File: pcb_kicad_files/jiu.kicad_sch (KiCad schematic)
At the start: 170 parts, among them J1 TYPE-C-31-M-12, J2 ARM JTAG, Q1 DTC123JKAT146, SW1 1U, SW10 1U, SW11 1U, SW12 1U, SW13 1U, SW14 1U, SW15 1U, SW16 2u, SW17 1.5U, SW18 1U, SW19 1U, SW2 1U, SW20 1U, SW21 1U, SW22 1U, SW23 1U, SW24 1U, SW25 1U, SW26 1U, SW27 1U, SW28 1U, SW29 1U, SW3 1U, SW30 1.5U, SW31 1U, SW32 1.75U, SW33 1U, SW34 1U, SW35 1U, SW36 1U, SW37 1U, SW38 1U, SW39 1U, SW4 1U, SW40 1U, SW41 1U, SW42 1U, SW43 1U, SW44 2.25U, SW45 1U, SW46 2.25U, SW47 1.25U, SW48 1U, SW49 1U, SW5 1U, SW50 1U, SW51 1U, SW52 1U, SW53 1U, SW54 1U, SW55 1U, SW56 1U, SW57 1.75U, SW58 1U, SW59 1U, SW6 1U, SW60 1.5U, SW61 1U, SW62 1.5U, SW63 7U, SW64 1U, SW65 1.5U, SW66 1U, SW67 K2-1187SQ-A4SW-06, SW68 1U, SW69 1U, SW7 1U, SW70 1.25U, SW71 1.25U, SW72 1.25U, SW73 6.25U, SW74 1.25U, SW8 1U, SW9 1U, U1 MCP1700T-3302E/TT, U2 STM32F072CBT6

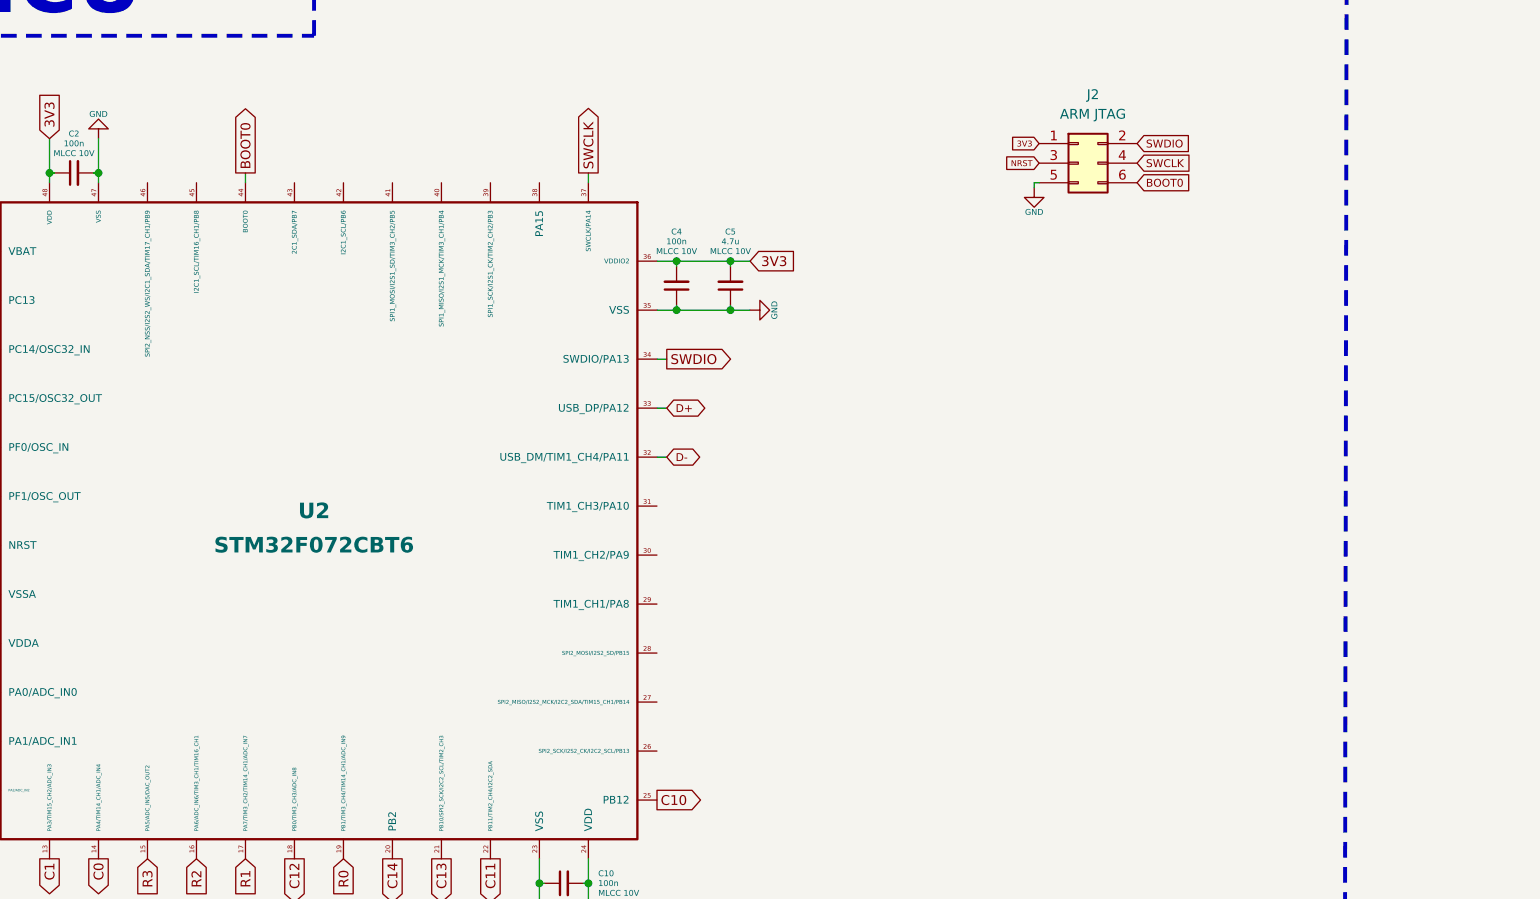
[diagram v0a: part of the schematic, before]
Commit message: Added pin header esposing extra unused MCU pins
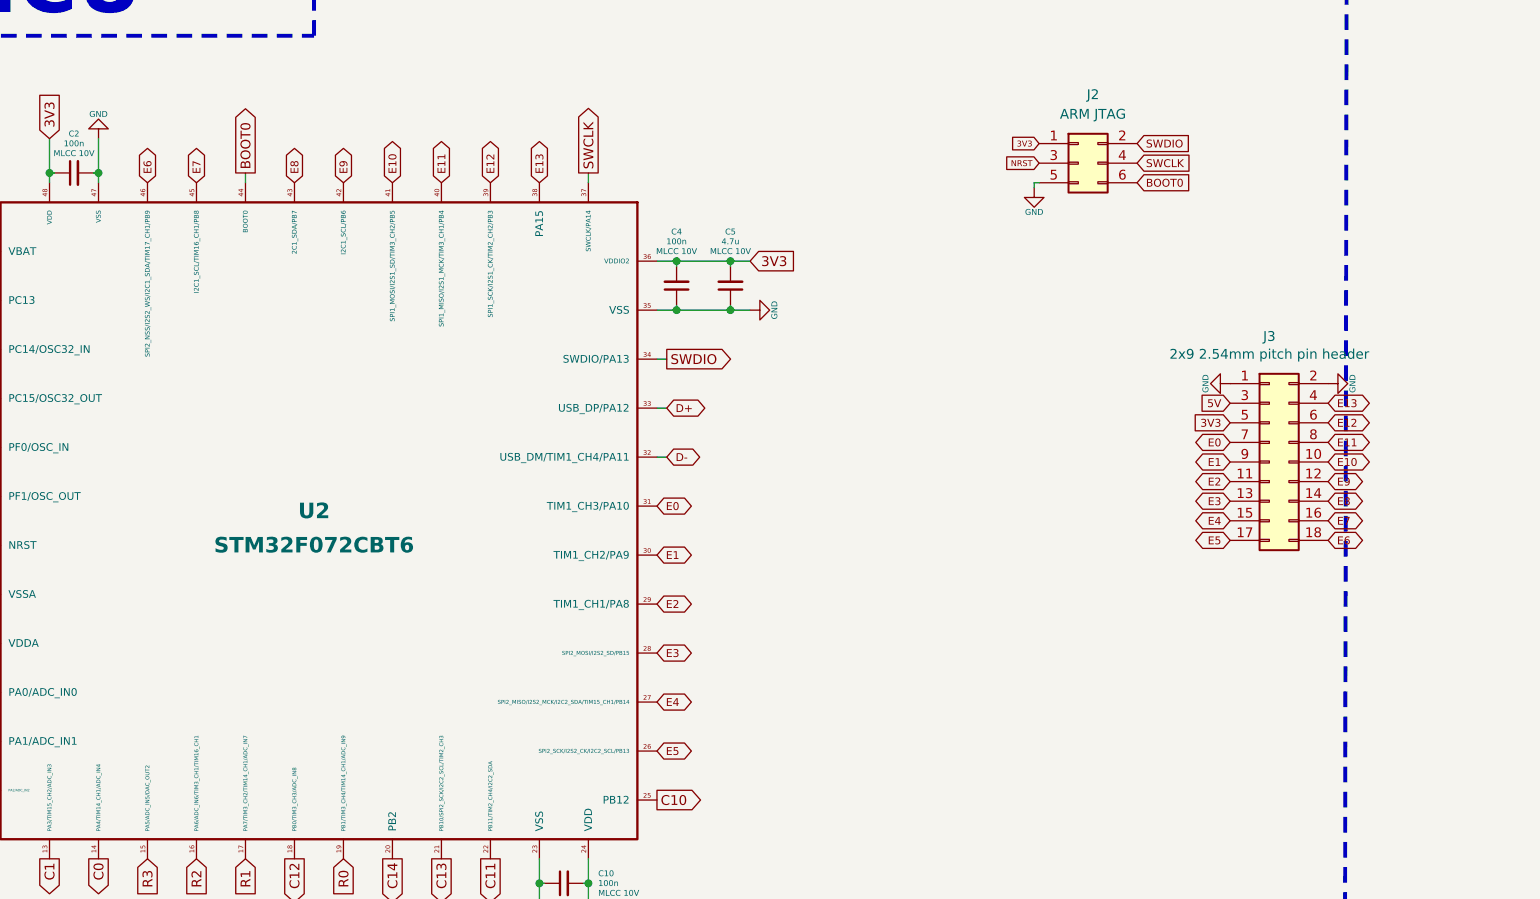
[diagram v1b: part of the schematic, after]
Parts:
- added J3: 2x9 2.54mm pitch pin header, acheron_Connectors:PinHeader_2x9_P2.54mm_Vertical, symbol Connector_Generic:Conn_02x09_Odd_Even
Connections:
- net 3V3: now also J3.5 (Pin_5)
- net 5V: now also J3.3 (Pin_3)
- net GND: now also J3.1 (Pin_1), J3.2 (Pin_2)
- net E5: now reaches U2.26 (SPI2_SCK/I2S2_CK/I2C2_SCL/PB13)
- net E5: now also J3.17 (Pin_17)
- net E4: now reaches U2.27 (SPI2_MISO/I2S2_MCK/I2C2_SDA/TIM15_CH1/PB14)
- net E4: now also J3.15 (Pin_15)
- net E3: now reaches U2.28 (SPI2_MOSI/I2S2_SD/PB15)
- net E3: now also J3.13 (Pin_13)
- net E2: now reaches U2.29 (TIM1_CH1/PA8)
- net E2: now also J3.11 (Pin_11)
- net E1: now reaches U2.30 (TIM1_CH2/PA9)
- net E1: now also J3.9 (Pin_9)
- net E0: now reaches U2.31 (TIM1_CH3/PA10)
- net E0: now also J3.7 (Pin_7)
- net E13: now reaches U2.38 (PA15)
- net E13: now also J3.4 (Pin_4)
- net E12: now reaches U2.39 (SPI1_SCK/I2S1_CK/TIM2_CH2/PB3)
- net E12: now also J3.6 (Pin_6)
- net E11: now reaches U2.40 (SPI1_MISO/I2S1_MCK/TIM3_CH1/PB4)
- net E11: now also J3.8 (Pin_8)
- net E10: now reaches U2.41 (SPI1_MOSI/I2S1_SD/TIM3_CH2/PB5)
- net E10: now also J3.10 (Pin_10)
- net E9: now reaches U2.42 (I2C1_SCL/PB6)
- net E9: now also J3.12 (Pin_12)
- net E8: now reaches U2.43 (2C1_SDA/PB7)
- net E8: now also J3.14 (Pin_14)
- net E7: now reaches U2.45 (I2C1_SCL/TIM16_CH1/PB8)
- net E7: now also J3.16 (Pin_16)
- net E6: now reaches U2.46 (SPI2_NSS/I2S2_WS/I2C1_SDA/TIM17_CH1/PB9)
- net E6: now also J3.18 (Pin_18)

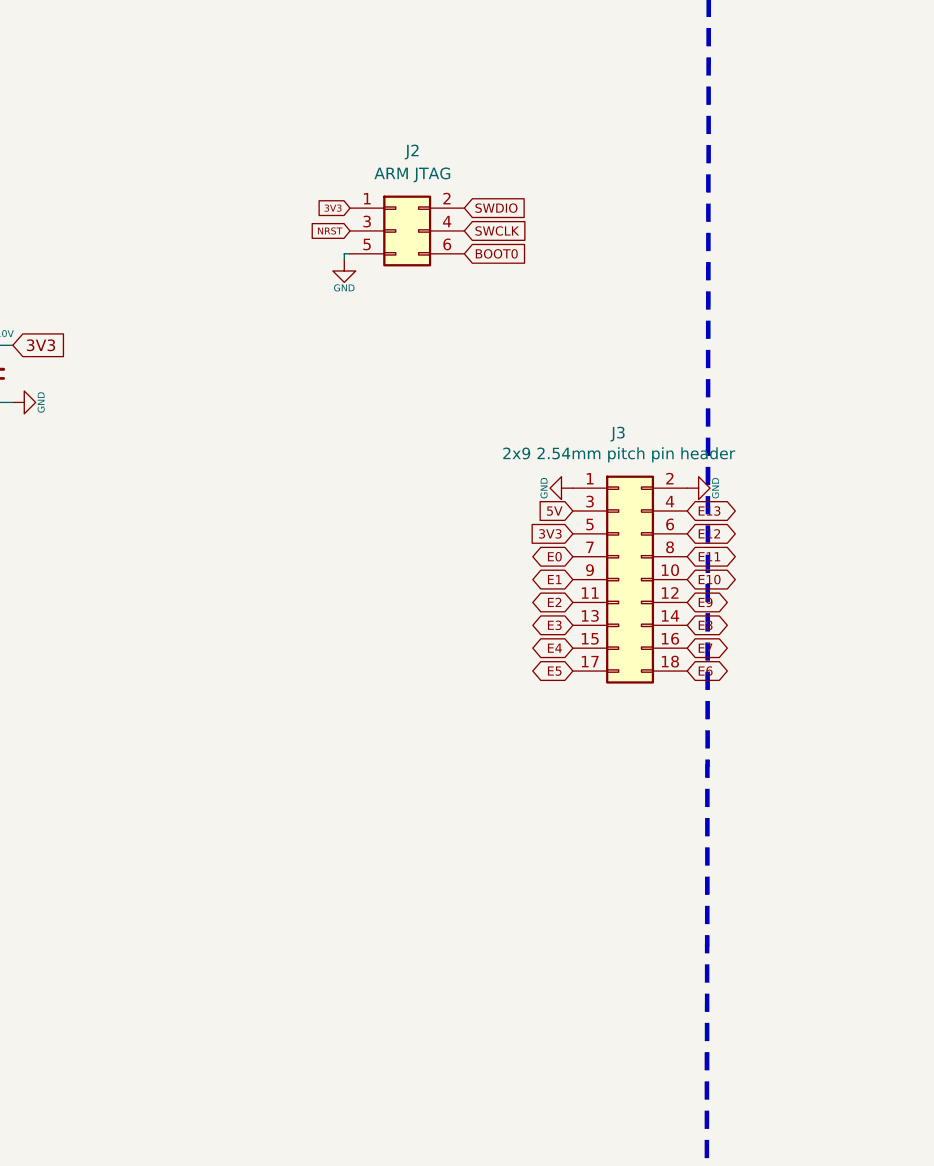
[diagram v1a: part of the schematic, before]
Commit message: Add pin header for rows
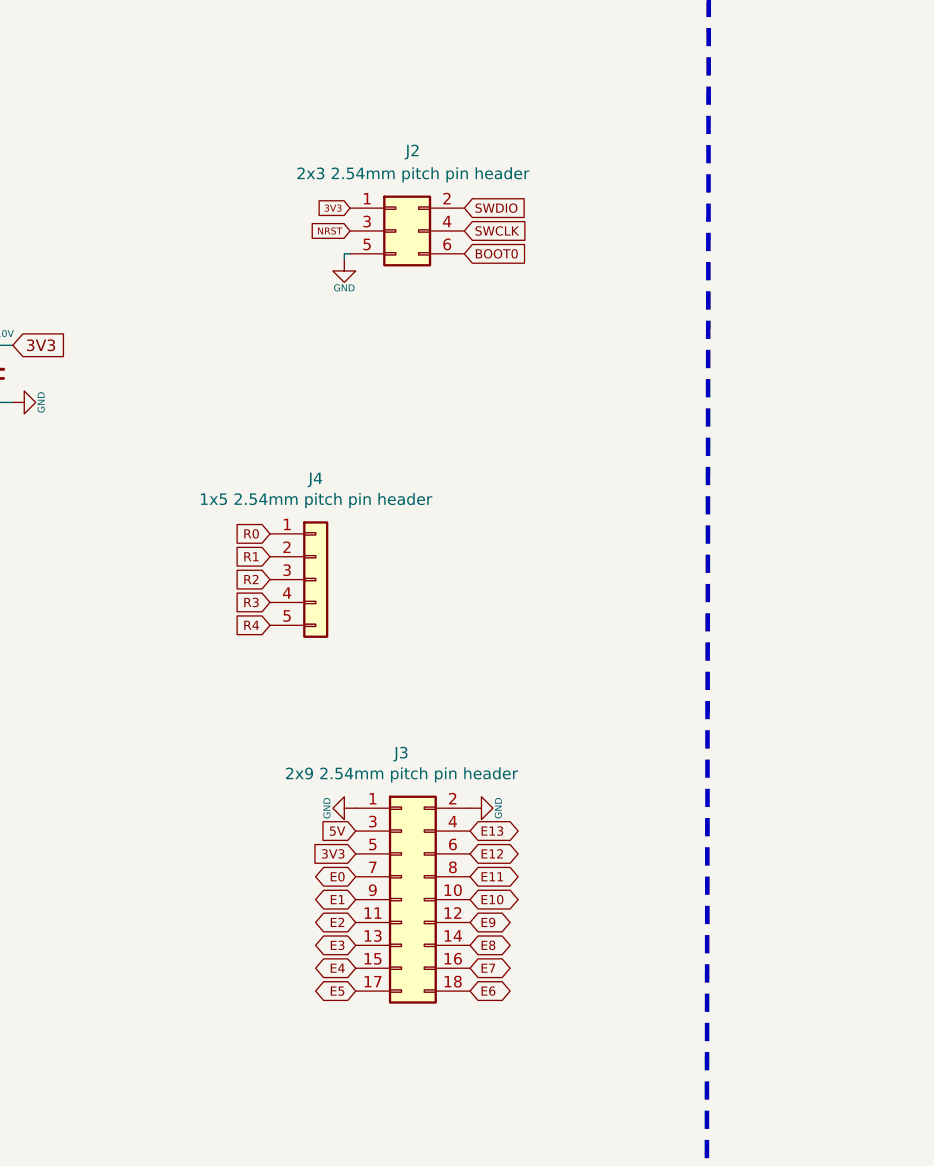
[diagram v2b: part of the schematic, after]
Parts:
- added J4: 1x5 2.54mm pitch pin header, acheron_Connectors:PinHeader_1x5_P2.54mm_Vertical, symbol Connector_Generic:Conn_01x05
- J2: value ARM JTAG -> 2x3 2.54mm pitch pin header
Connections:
- net R0: now also J4.1 (Pin_1)
- net R1: now also J4.2 (Pin_2)
- net R2: now also J4.3 (Pin_3)
- net R3: now also J4.4 (Pin_4)
- net R4: now also J4.5 (Pin_5)
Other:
- moved on the sheet: J3

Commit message: Added USBLC chip, removed discrete TVS, organized LDO circuitry
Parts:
- removed D17: SMF6.0A, acheron_Components:D_SOD-123, symbol Device:D_Schottky
- added U1: USBLC6-2SC6, acheron_Components:SOT-23-6, symbol Power_Protection:USBLC6-2SC6
- renumbered C7 to C10, C10 to C11, C11 to C12, C12 to C4, C4 to C5, C5 to C6, C8 to C7, C9 to C8, C6 to C9, D11 to D10, D12 to D11, D14 to D12, D15 to D13, D16 to D14, D18 to D15, D19 to D16, D20 to D17, D21 to D18, D22 to D19, D23 to D20, D25 to D21, D26 to D22, D27 to D23, D28 to D24, D29 to D25, D30 to D26, D32 to D27, D33 to D28, D35 to D29, D36 to D30, D37 to D31, D38 to D32, D39 to D33, D40 to D34, D41 to D35, D42 to D36, D44 to D37, D45 to D38, D46 to D39, D47 to D40, D48 to D41, D50 to D42, D51 to D43, D53 to D44, D54 to D45, D55 to D46, D56 to D47, D57 to D48, D58 to D49, D60 to D50, D61 to D51, D62 to D52, D63 to D53, D64 to D54, D65 to D55, D66 to D56, D78 to D57, D69 to D58, D70 to D59, D7 to D6, D71 to D60, D72 to D61, D73 to D62, D75 to D63, D80 to D64, D76 to D65, D82 to D66, D6 to D67, D13 to D68, D8 to D7, D9 to D8, D10 to D9, J2 to J1, J1 to J2, J4 to J3, J3 to J4, R3 to R1, R1 to R2, R2 to R3, SW47 to SW46, SW46 to SW47, SW59 to SW48, SW48 to SW49, SW49 to SW50, SW50 to SW51, SW51 to SW52, SW52 to SW53, SW53 to SW54, SW54 to SW55, SW55 to SW56, SW56 to SW57, SW57 to SW58, SW68 to SW59, SW58 to SW60, SW60 to SW61, SW61 to SW62, SW62 to SW63, SW63 to SW64, SW69 to SW66, SW64 to SW67, SW66 to SW68, SW70 to SW69, SW71 to SW70, SW72 to SW71, SW73 to SW72, SW74 to SW73, SW67 to SW74, U1 to U3
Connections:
- net D+: now also U1.3 (I/O2); no longer J2.A6 (D+), J2.B6 (D+)
- net D-: now also U1.1 (I/O1); no longer J2.A7 (D-), J2.B7 (D-)
- net GND: now also U1.2 (GND)
- net VUSB: now also U1.5 (VBUS)
- new net DBUS+: J2.A6 (D+), J2.B6 (D+), U1.4 (I/O2)
- new net DBUS-: J2.A7 (D-), J2.B7 (D-), U1.6 (I/O1)

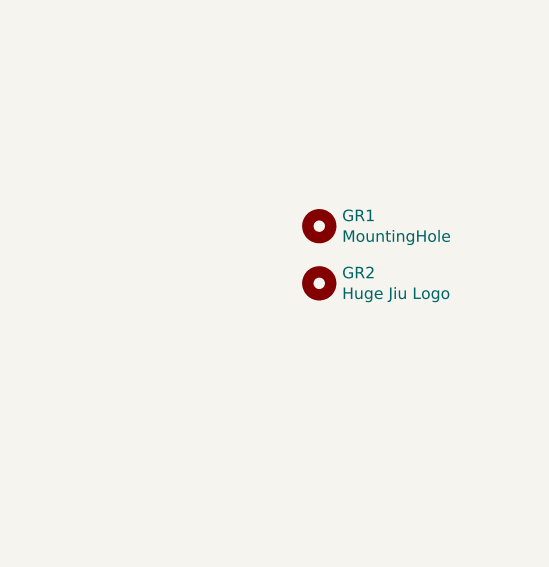
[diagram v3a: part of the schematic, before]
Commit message: Add Acheron Plated logo to PCB front
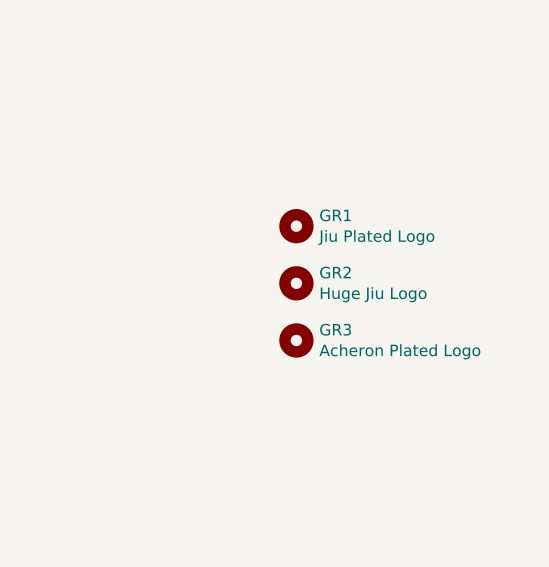
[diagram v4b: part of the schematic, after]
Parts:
- added GR3: Acheron Plated Logo, acheron_Logos:acheronShort_0.3x0.5in_Plated, symbol Mechanical:MountingHole
- GR1: value MountingHole -> Jiu Plated Logo
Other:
- moved on the sheet: GR1, GR2
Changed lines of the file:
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@@
     (title "Jiu schematic")
     (date "2021-01-13")
-    (rev "v1.1.2")
+    (rev "v1.1.3-c1")
     (company "Designed by Gondolindrim")
   )
@@
     )
   )
-  (symbol (lib_id "Mechanical:MountingHole") (at 497.84 171.45 0) (unit 1)
+  (symbol (lib_id "Mechanical:MountingHole") (at 495.3 171.45 0) (unit 1)
     (in_bom no) (on_board yes)
-    (property "Reference" "GR1" (id 0) (at 500.3801 170.3006 0)
+    (property "Reference" "GR1" (id 0) (at 497.8401 170.3006 0)
       (effects (font (size 1.27 1.27)) (justify left))
     )
-    (property "Value" "MountingHole" (id 1) (at 500.3801 172.5993 0)
+    (property "Value" "Jiu Plated Logo" (id 1) (at 497.8401 172.5993 0)
       (effects (font (size 1.27 1.27)) (justify left))
     )
-    (property "Footprint" "jiu_graphics:jiu_logo_15.9x15.0mm" (id 2) (at 497.84 171.45 0)
+    (property "Footprint" "jiu_graphics:jiu_logo_15.9x15.0mm" (id 2) (at 495.3 171.45 0)
       (effects (font (size 1.27 1.27)) hide)
     )
-    (property "Datasheet" "~" (id 3) (at 497.84 171.45 0)
+    (property "Datasheet" "~" (id 3) (at 495.3 171.45 0)
       (effects (font (size 1.27 1.27)) hide)
     )
   )
-  (symbol (lib_id "Mechanical:MountingHole") (at 497.84 177.8 0) (unit 1)
+  (symbol (lib_id "Mechanical:MountingHole") (at 495.3 177.8 0) (unit 1)
     (in_bom no) (on_board yes)
-    (property "Reference" "GR2" (id 0) (at 500.3801 176.6506 0)
+    (property "Reference" "GR2" (id 0) (at 497.8401 176.6506 0)
       (effects (font (size 1.27 1.27)) (justify left))
     )
-    (property "Value" "Huge Jiu Logo" (id 1) (at 500.3801 178.9493 0)
+    (property "Value" "Huge Jiu Logo" (id 1) (at 497.8401 178.9493 0)
       (effects (font (size 1.27 1.27)) (justify left))
     )
-    (property "Footprint" "jiu_graphics:jiu_logo_80x75.6" (id 2) (at 497.84 177.8 0)
+    (property "Footprint" "jiu_graphics:jiu_logo_80x75.6" (id 2) (at 495.3 177.8 0)
       (effects (font (size 1.27 1.27)) hide)
     )
-    (property "Datasheet" "~" (id 3) (at 497.84 177.8 0)
+    (property "Datasheet" "~" (id 3) (at 495.3 177.8 0)
+      (effects (font (size 1.27 1.27)) hide)
+    )
+  )
+  (symbol (lib_id "Mechanical:MountingHole") (at 495.3 184.15 0) (unit 1)
+    (in_bom no) (on_board yes)
+    (property "Reference" "GR3" (id 0) (at 497.8401 183.0006 0)
+      (effects (font (size 1.27 1.27)) (justify left))
+    )
+    (property "Value" "Acheron Plated Logo" (id 1) (at 497.8401 185.2993 0)
+      (effects (font (size 1.27 1.27)) (justify left))
+    )
+    (property "Footprint" "acheron_Logos:acheronShort_0.3x0.5in_Plated" (id 2) (at 495.3 184.15 0)
+      (effects (font (size 1.27 1.27)) hide)
+    )
+    (property "Datasheet" "~" (id 3) (at 495.3 184.15 0)
       (effects (font (size 1.27 1.27)) hide)
     )
@@
     )
     (path "/0eef0c02-56dd-4af2-ab7e-8a661a917c89"
-      (reference "GR1") (unit 1) (value "MountingHole") (footprint "jiu_graphics:jiu_logo_15.9x15.0mm")
+      (reference "GR1") (unit 1) (value "Jiu Plated Logo") (footprint "jiu_graphics:jiu_logo_15.9x15.0mm")
     )
     (path "/c3a789f0-1bd3-4731-a466-0502f1b91899"
       (reference "GR2") (unit 1) (value "Huge Jiu Logo") (footprint "jiu_graphics:jiu_logo_80x75.6")
     )
+    (path "/595c22e3-12a7-4ffb-b454-35a27f64443c"
+      (reference "GR3") (unit 1) (value "Acheron Plated Logo") (footprint "acheron_Logos:acheronShort_0.3x0.5in_Plated")
+    )
     (path "/aecb07b2-9d27-41eb-8320-1ebe9ea13f34"

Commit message: Added metadata to some components
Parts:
- J2: LCSC Part Number (none) -> C165948; Manufacturer (none) -> Korean Hroparts; Manufacturer Part Number (none) -> TYPE-C-31-M-12; Specification (none) -> USB type C female 16 pin connector
- Q1: LCSC Part Number (none) -> C111724; Specification (none) -> NPN pre-biased 200mW BJT transistor
- U1: LCSC Part Number (none) -> C7519; Manufacturer (none) -> STMicroelectronics; Manufacturer Part Number (none) -> USBLC6-2SC6; Package (none) -> SOT-23-6; Specification (none) -> Unidirectional 6V 5A SOT-23-6 TVS diode for USB ESD protect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
- U2: Specification (none) -> 32-bit 128kB FLASH ARM Cortex-M0 48MHz
- U3: Specification (none) -> Fixed 3.3V low dropout regulator
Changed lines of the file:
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@@
     (title "Jiu schematic")
     (date "2021-01-13")
-    (rev "v1.1.3-c1")
+    (rev "v1.1.3-c2")
     (company "Designed by Gondolindrim")
   )
@@
       (effects (font (size 1.27 1.27)) hide)
     )
+    (property "LCSC Part Number" "C111724" (id 4) (at 187.325 267.97 0)
+      (effects (font (size 1.27 1.27)) hide)
+    )
+    (property "Specification" "NPN pre-biased 200mW BJT transistor" (id 5) (at 187.325 267.97 0)
+      (effects (font (size 1.27 1.27)) hide)
+    )
   )
   (symbol (lib_id "Regulator_Linear:MCP1700-3302E_SOT23") (at 204.47 334.645 0) (unit 1)
@@
       (effects (font (size 1.27 1.27)) hide)
     )
+    (property "Specification" "Fixed 3.3V low dropout regulator" (id 4) (at 204.47 334.645 0)
+      (effects (font (size 1.27 1.27)) hide)
+    )
   )
   (symbol (lib_id "acheronSymbols:MXSwitch") (at 50.8 50.8 90) (mirror x) (unit 1)
@@
       (effects (font (size 1.27 1.27)) hide)
     )
+    (property "LCSC Part Number" "C7519" (id 4) (at 52.705 239.395 0)
+      (effects (font (size 1.27 1.27)) hide)
+    )
+    (property "Manufacturer" "STMicroelectronics" (id 5) (at 52.705 239.395 0)
+      (effects (font (size 1.27 1.27)) hide)
+    )
+    (property "Manufacturer Part Number" "USBLC6-2SC6" (id 6) (at 52.705 239.395 0)
+      (effects (font (size 1.27 1.27)) hide)
+    )
+    (property "Package" "SOT-23-6" (id 7) (at 52.705 239.395 0)
+      (effects (font (size 1.27 1.27)) hide)
+    )
+    (property "Specification" "Unidirectional 6V 5A SOT-23-6 TVS diode for USB ESD protection" (id 8) (at 52.705 239.395 0)
+      (effects (font (size 1.27 1.27)) hide)
+    )
   )
   (symbol (lib_id "acheronSymbols:TYPE-C-31-M12_13") (at 99.06 289.56 0) (unit 1)
@@
       (effects (font (size 1.524 1.524)) hide)
     )
+    (property "LCSC Part Number" "C165948" (id 4) (at 99.06 289.56 0)
+      (effects (font (size 1.27 1.27)) hide)
+    )
+    (property "Manufacturer" "Korean Hroparts" (id 5) (at 99.06 289.56 0)
+      (effects (font (size 1.27 1.27)) hide)
+    )
+    (property "Manufacturer Part Number" "TYPE-C-31-M-12" (id 6) (at 99.06 289.56 0)
+      (effects (font (size 1.27 1.27)) hide)
+    )
+    (property "Specification" "USB type C female 16 pin connector" (id 7) (at 99.06 289.56 0)
+      (effects (font (size 1.27 1.27)) hide)
+    )
   )
   (symbol (lib_id "acheronSymbols:STM32F072-LQFP48") (at 316.865 323.215 0) (unit 1)
@@
       (effects (font (size 1.27 1.27)) hide)
     )
+    (property "Specification" "32-bit 128kB FLASH ARM Cortex-M0 48MHz " (id 4) (at 316.865 323.215 0)
+      (effects (font (size 1.27 1.27)) hide)
+    )
